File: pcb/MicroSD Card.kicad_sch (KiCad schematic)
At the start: 6 parts, among them J4 Micro_SD_Card

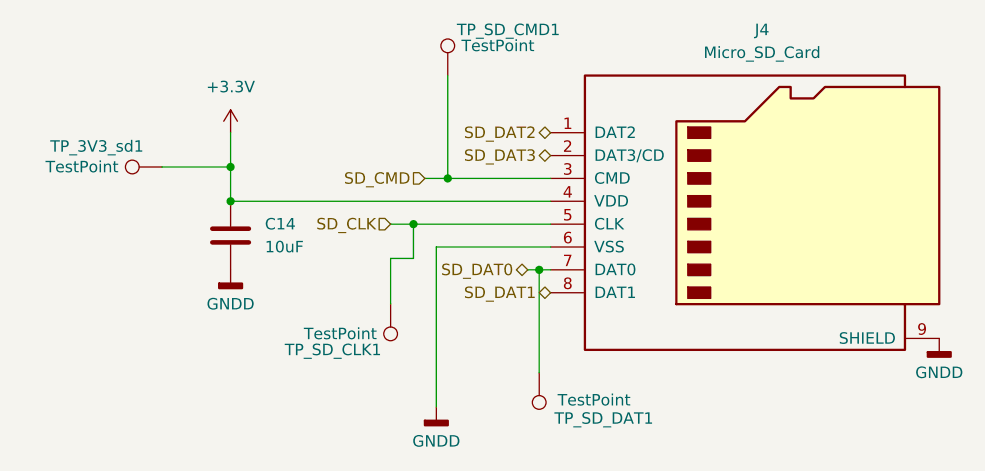
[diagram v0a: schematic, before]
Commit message: Updated schematics and removed most test points
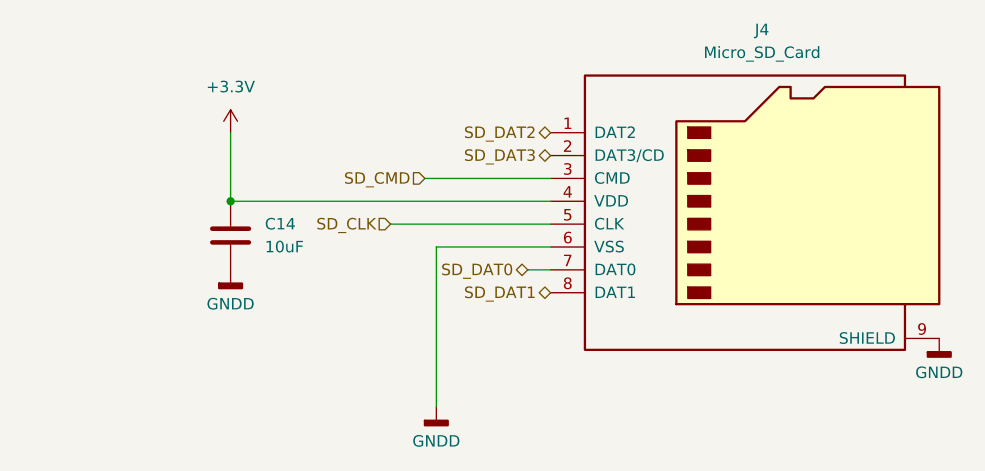
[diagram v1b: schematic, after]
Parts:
- removed TP_3V3_sd1, TP_SD_CLK1, TP_SD_CMD1, TP_SD_DAT1: TestPoint, TestPoint:TestPoint_Loop_D2.54mm_Drill1.5mm_Beaded, symbol Connector:TestPoint
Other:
- title: Ride-Along Module -> Control Module Rev2
